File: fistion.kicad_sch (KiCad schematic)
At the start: 37 parts, among them J1 debug-port, K1 diode-choc, K10 diode-choc, K11 diode-choc, K12 diode-choc, K13 diode-choc, K14 diode-choc, K15 diode-choc, K16 diode-choc, K2 diode-choc, K3 diode-choc, K4 diode-choc, K5 diode-choc, K6 diode-choc, K7 diode-choc, K8 diode-choc, K9 diode-choc, SW1 SW_Push, U1 MT25QL128ABA1ESE, U2 ms88sf3-nrf52840

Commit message: routed
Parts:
- removed D1: D_Small, Diode_SMD:D_SOD-123, symbol Device:D_Small
- added C10, C11: 100nF, Capacitor_SMD:C_0603_1608Metric, symbol Device:C_Small
- added C12: 100uF, Capacitor_SMD:C_0603_1608Metric, symbol Device:C_Small
- added C13, C15: 10nF, Capacitor_SMD:C_0603_1608Metric, symbol Device:C_Small
- added C14: 10uF, Capacitor_SMD:C_0603_1608Metric, symbol Device:C_Small
- added C3, C9: 100nF, Capacitor_SMD:C_0603_1608Metric, symbol Device:C
- added J10, J3, J4, J5, J6, J7, J8, J9: Conn_01x06_Male, fistion:bridge, symbol Connector:Conn_01x06_Male
- added JP2: jumper, Jumper:SolderJumper-3_P1.3mm_Open_RoundedPad1.0x1.5mm, symbol Jumper:SolderJumper_3_Open
- added SC1: solar, misc:KXOB25-05X3F, symbol Device:Solar_Cell
- added U3: LSM6DS3, Package_LGA:LGA-14_3x2.5mm_P0.5mm_LayoutBorder3x4y, symbol Sensor_Motion:LSM6DS3
- added U8: PMW3610, sensor:PMW3610, symbol sensor:PMW3610
- added U9: MCP1804x-1802xMB, Package_TO_SOT_SMD:SOT-89-3, symbol Regulator_Linear:MCP1804x-1802xMB
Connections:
- net C0_LEFT is gone; now on net R3: U2.41 (P0.17)
- net C4 is gone; now on net R0: U2.44 (P0.20)
- net IR_EN is gone; now on net DISP_~{CS}: U2.21 (P1.08)
- net BAT_MEAS: now also U2.9 ([L]_A0_P0.02); no longer U2.16 (A2_P0.04)
- net C0: now also J5.1 (Pin_1); no longer K13.2
- net C2: now also J8.1 (Pin_1); no longer K15.2
- net C3: now also J8.2 (Pin_2); no longer K16.2
- net DISP_~{CS}: no longer U2.38 (P0.19)
- net FLASH_~{CS}: now also U2.14 (P0.27); no longer U2.26 (P1.09)
- net GND: now also C10.1, C11.1, C13.2, C14.2, C15.2, C3.2, C9.2, J8.6 (Pin_6), U3.2 (SDX), U3.3 (SCX), U3.6 (GND), U3.7 (GND), U8.11 (GND), U9.2 (GND)
- net MISO_DQ1: now also U2.15 (A3_P0.05), U3.1 (SDO/SA0); no longer U2.25 (P0.08)
- net MOSI_DQ0: now also U2.16 (A2_P0.04), U3.14 (SDA); no longer U2.27 (P0.12)
- net R0: no longer U2.43 (P0.23)
- net R1: now also U2.43 (P0.23); no longer U2.42 (P0.21)
- net R2: now also U2.42 (P0.21); no longer U2.9 ([L]_A0_P0.02)
- net R3: now also J5.2 (Pin_2), J8.3 (Pin_3); no longer K13.1, K15.1, K16.1, U2.19 (P0.07)
- net SCLK: now also U2.17 (P0.26), U3.13 (SCL); no longer U2.29 (P0.16)
- net VDDH: now also JP2.1 (A)
- net ~{BLUE}: now also U2.2 ([L]_P1.11); no longer U2.12 ([L]_A6_P0.30)
- net ~{GREEN}: now also U2.3 ([L]_P1.12); no longer U2.11 ([L]_A4_P0.28)
- net ~{RED}: now also U2.4 ([L]_P1.10); no longer U2.10 ([L]_A5_P0.29)
- net at R4.2: now also J5.5 (Pin_5); no longer D2.1 (RK)
- net at R6.2: now also J5.3 (Pin_3); no longer D2.3 (BK)
- net at R5.2: now also J5.4 (Pin_4); no longer D2.4 (GK)
- net 3V3 renamed +3V3
- net +3V3: now also C10.2, C3.1, C9.1, J5.6 (Pin_6), JP2.3 (B), U3.5 (VDDIO), U3.8 (VDD), U8.6 (VDDIO); no longer D2.2 (A)
- net ENC_OUT: no longer names the net of U2.22 (P0.11)
- net IO_INT: no longer names the net of U2.40 (P0.15)
- net IO_~{CS}: no longer names the net of U2.39 (P0.13)
- net MID_BTN renamed IMU_INT
- net IMU_INT: now also U3.9 (INT2)
- net TP_DR renamed MOUSE_~{RST}
- net MOUSE_~{RST}: now also U8.7 (~{RESET})
- net TP_~{CS} renamed MOTION
- net MOTION: now also U8.8 (MOTION)
- new net: J9.3 (Pin_3), K16.1
- new net: J9.2 (Pin_2), K16.2
- new net: J3.1 (Pin_1), J6.1 (Pin_1), K13.2
- new net: J3.2 (Pin_2), J6.2 (Pin_2), K13.1
- new net: J3.3 (Pin_3), J6.3 (Pin_3)
- new net: J3.4 (Pin_4), J6.4 (Pin_4)
- new net: J3.5 (Pin_5), J6.5 (Pin_5)
- new net: J3.6 (Pin_6), J6.6 (Pin_6)
- new net: D2.3 (BK), J4.3 (Pin_3)
- new net: D2.4 (GK), J4.4 (Pin_4)
- new net: D2.1 (RK), J4.5 (Pin_5)
- new net: D2.2 (A), J4.6 (Pin_6)
- new net: J9.5 (Pin_5), SC1.1 (+)
- new net: J9.6 (Pin_6), SC1.2 (-)
- new net: C13.1, U8.1 (+VCSEL), U8.10 (PASS_T)
- new net: C12.2, U8.12 (C+)
- new net: C12.1, U8.13 (C-)
- new net: U8.15 (XYLASER), U8.16 (-VCSEL)
- new net: C14.1, C15.1, U8.9 (VCP)
- new net: J10.3 (Pin_3), J7.3 (Pin_3), K15.1
- new net: J10.1 (Pin_1), J7.1 (Pin_1), K15.2
- new net: JP2.2 (C), U9.3 (IN)
- new net: J10.2 (Pin_2), J7.2 (Pin_2)
- new net: J10.5 (Pin_5), J7.5 (Pin_5)
- new net: J10.6 (Pin_6), J7.6 (Pin_6)
- new net +1V8: C11.2, U8.14 (VDD), U9.1 (OUT)
- new net IMU_~{CS}: U2.19 (P0.07), U3.12 (CS)
- new net MOUSE_~{CS}: U2.25 (P0.08), U8.5 (~{CS})
- new net SCLK2: U2.26 (P1.09), U8.3 (SCLK)
- new net SDIO: U2.27 (P0.12), U8.2 (SDIO)
- new net SOLAR: J8.5 (Pin_5)
- no-connect marks 9 -> 18
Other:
- sheet power ports: added none; removed GND, MAGNET
- note added: "- capacitive for hand detection"
- note removed: "- prox sensors for idle & mouse detection? - the actual mouse - IMU"
- moved on the sheet: D2, JP1, K1, K10, K11, K12, K13, K14, K15, K16, K2, K3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

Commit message: no screen
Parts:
- removed JP2: jumper, Jumper:SolderJumper-3_P1.3mm_Open_RoundedPad1.0x1.5mm, symbol Jumper:SolderJumper_3_Open
- removed LCD1: adafruit-sharp-memory-display-no-useless, display:adafruit-sharp-memory-display-1.3in-no-mounting-no-useless, symbol display:adafruit-sharp-memory-display-no-useless
- added SW2: RotaryEncoder_Switch, switch:EVQWGD001, symbol Device:RotaryEncoder_Switch
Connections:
- net +3V3: no longer C10.2, C2.1, C3.1, C9.1, J1.2 (3V3), L1.2, U2.31 (VDD), U3.5 (VDDIO), U3.8 (VDD), U8.6 (VDDIO)
- net GND: now also SW2.C, SW2.S1
- net MOTION: now also U2.22 (P0.11); no longer U2.23 (P0.00)
- net MOUSE_~{CS}: now also U2.24 (P0.01); no longer U2.25 (P0.08)
- net MOUSE_~{RST}: now also U2.23 (P0.00); no longer U2.24 (P0.01)
- net SCLK2: now also U2.25 (P0.08); no longer U2.26 (P1.09)
- net SDIO: now also U2.26 (P1.09); no longer U2.27 (P0.12)
- net VDDH: now also U9.3 (IN)
- net A: now reaches U2.29 (P0.16)
- net A: now also SW2.A
- net ENC_PUSH: now reaches U2.30 (P0.14)
- net ENC_PUSH: now also SW2.S2
- net DISP_~{CS}: no longer names the net of U2.21 (P1.08)
- new net 3V3_nRF: C10.2, C2.1, C3.1, C9.1, J1.2 (3V3), L1.2, U2.31 (VDD), U3.5 (VDDIO), U3.8 (VDD), U8.6 (VDDIO)
- new net B: SW2.B, U2.27 (P0.12)
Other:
- moved on the sheet: U9

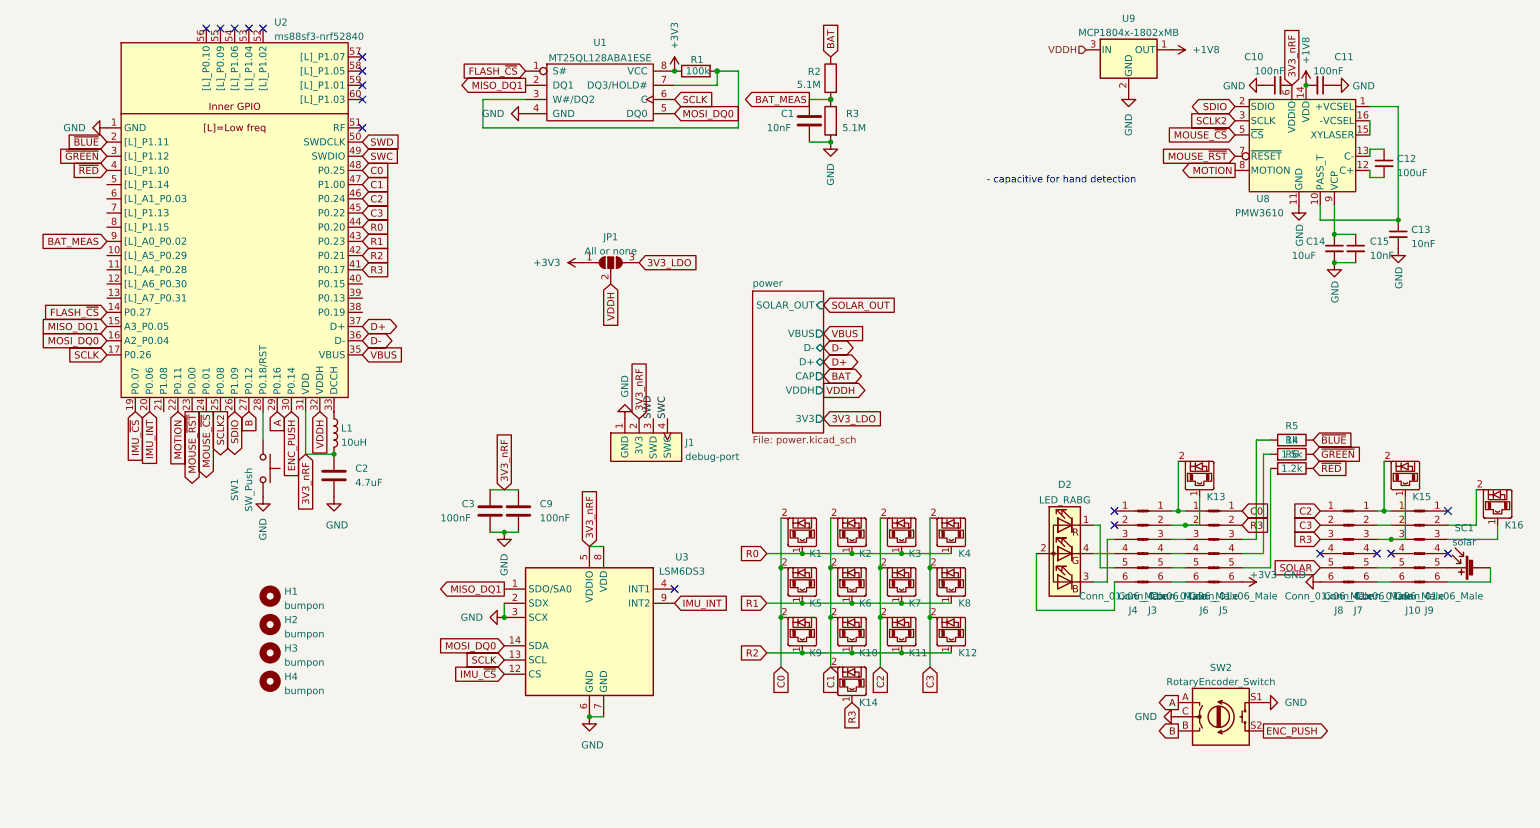
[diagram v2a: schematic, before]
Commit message: scroll wheel + constant current charger
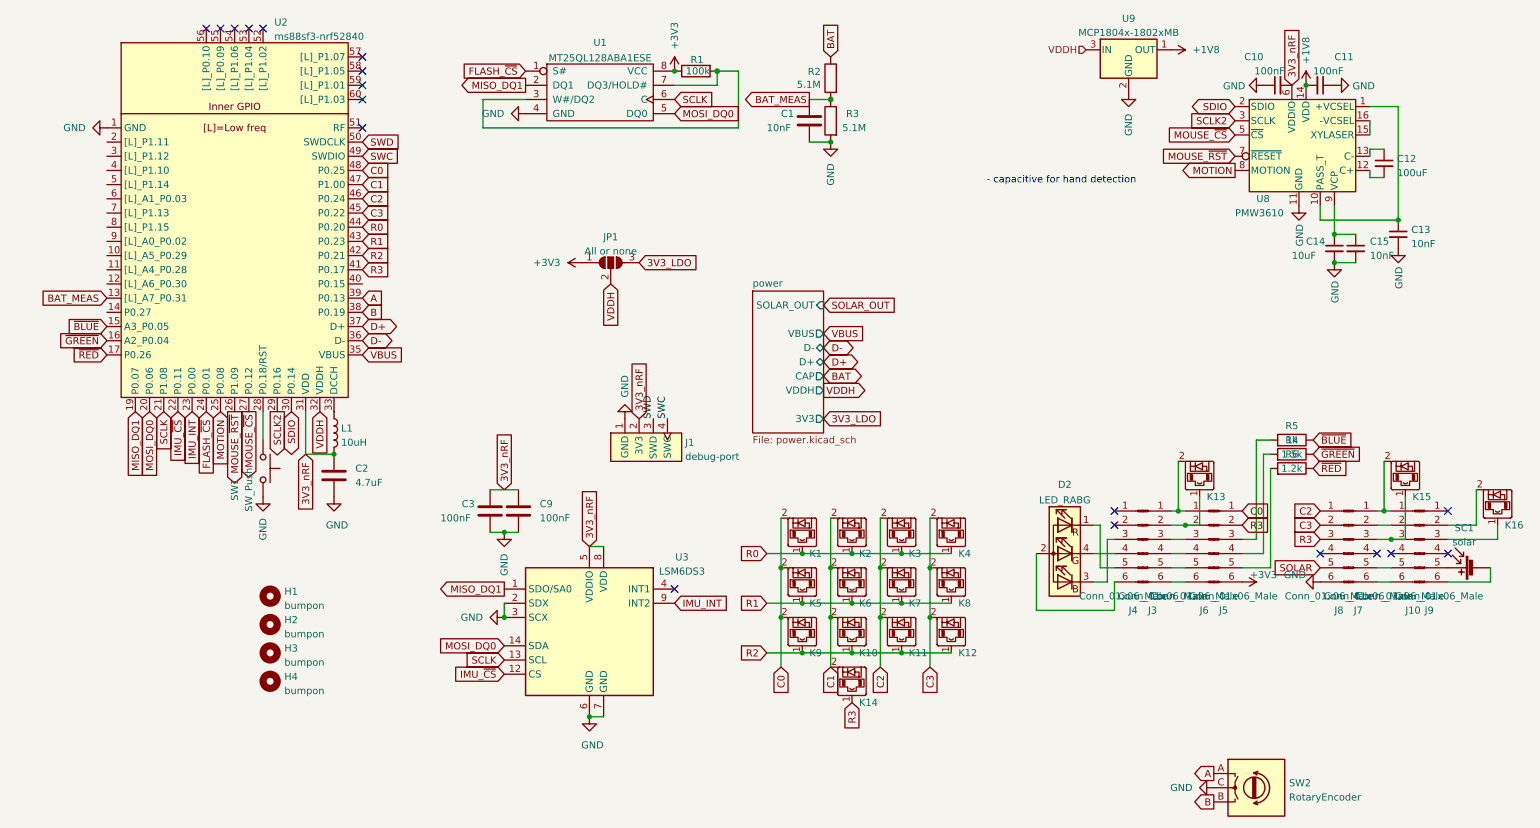
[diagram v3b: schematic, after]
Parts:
- removed SW2: RotaryEncoder_Switch, switch:EVQWGD001, symbol Device:RotaryEncoder_Switch
- added SW2: RotaryEncoder, switch:EC10E, symbol Device:RotaryEncoder
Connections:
- net ENC_PUSH is gone; now on net SDIO: U2.30 (P0.14)
- net A: now also U2.39 (P0.13), SW2.A; no longer U2.29 (P0.16)
- net B: now also U2.38 (P0.19), SW2.B; no longer U2.27 (P0.12)
- net BAT_MEAS: now also U2.13 ([L]_A7_P0.31); no longer U2.9 ([L]_A0_P0.02)
- net FLASH_~{CS}: now also U2.24 (P0.01); no longer U2.14 (P0.27)
- net GND: now also SW2.C
- net IMU_INT: now also U2.23 (P0.00); no longer U2.20 (P0.06)
- net IMU_~{CS}: now also U2.22 (P0.11); no longer U2.19 (P0.07)
- net MISO_DQ1: now also U2.19 (P0.07); no longer U2.15 (A3_P0.05)
- net MOSI_DQ0: now also U2.20 (P0.06); no longer U2.16 (A2_P0.04)
- net MOTION: now also U2.25 (P0.08); no longer U2.22 (P0.11)
- net MOUSE_~{CS}: now also U2.27 (P0.12); no longer U2.24 (P0.01)
- net MOUSE_~{RST}: now also U2.26 (P1.09); no longer U2.23 (P0.00)
- net SCLK: now also U2.21 (P1.08); no longer U2.17 (P0.26)
- net SCLK2: now also U2.29 (P0.16); no longer U2.25 (P0.08)
- net SDIO: no longer U2.26 (P1.09)
- net ~{BLUE}: now also U2.15 (A3_P0.05); no longer U2.2 ([L]_P1.11)
- net ~{GREEN}: now also U2.16 (A2_P0.04); no longer U2.3 ([L]_P1.12)
- net ~{RED}: now also U2.17 (P0.26); no longer U2.4 ([L]_P1.10)

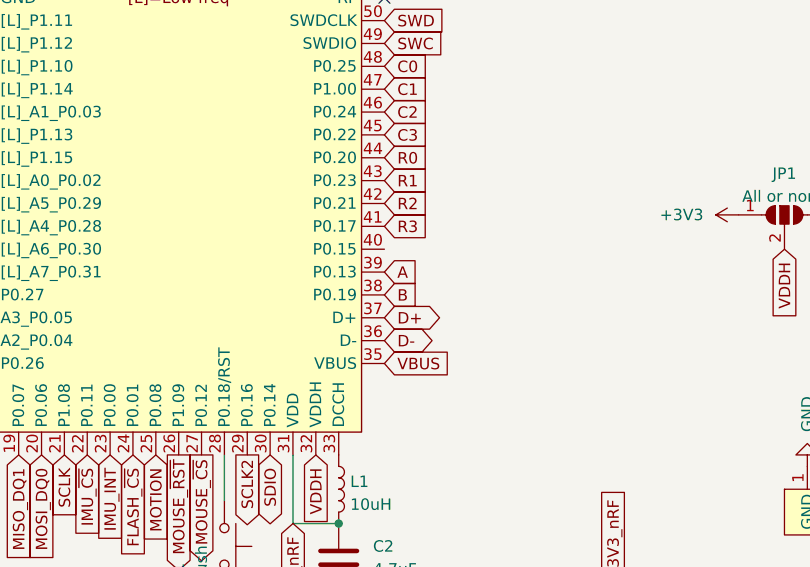
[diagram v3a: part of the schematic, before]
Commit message: routed with encoder model
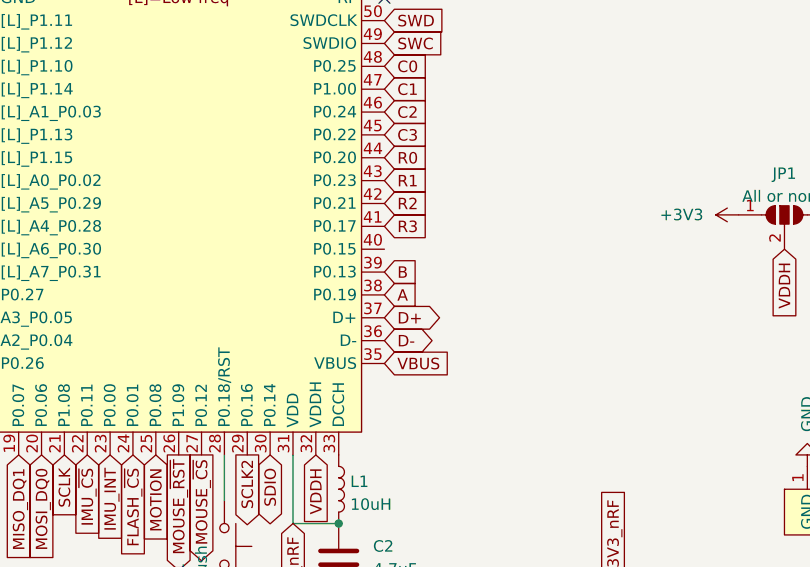
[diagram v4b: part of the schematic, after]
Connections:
- net A: now also U2.38 (P0.19); no longer U2.39 (P0.13)
- net B: now also U2.39 (P0.13); no longer U2.38 (P0.19)
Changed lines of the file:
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@@
     )
   )
-  (global_label "A" (shape input) (at 74.93 72.39 0) (fields_autoplaced)
+  (global_label "A" (shape input) (at 74.93 74.93 0) (fields_autoplaced)
     (effects (font (size 1.27 1.27)) (justify left))
-    (property "Intersheet References" "${INTERSHEET_REFS}" (id 0) (at 78.6222 72.3106 0)
+    (property "Intersheet References" "${INTERSHEET_REFS}" (id 0) (at 78.6222 75.0094 0)
       (effects (font (size 1.27 1.27)) (justify left) hide)
     )
@@
     )
   )
-  (global_label "B" (shape input) (at 74.93 74.93 0) (fields_autoplaced)
+  (global_label "B" (shape input) (at 74.93 72.39 0) (fields_autoplaced)
     (effects (font (size 1.27 1.27)) (justify left))
-    (property "Intersheet References" "${INTERSHEET_REFS}" (id 0) (at 78.8036 74.8506 0)
+    (property "Intersheet References" "${INTERSHEET_REFS}" (id 0) (at 78.8036 72.4694 0)
       (effects (font (size 1.27 1.27)) (justify left) hide)
     )
